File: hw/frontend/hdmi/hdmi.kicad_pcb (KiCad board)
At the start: 6 copper layers, 100 x 100 mm, 208 parts, among them J801 SAMTEC_QSH-090-D, P201 HDMI, P301 HDMI, P302 CONN_02X05, P601 CONN_02X03, P602 CONN_02X05, P801 CONN_01X02, U202 TPD12S520, U301 TPD12S521, U302 PTN3360DBS, U401 TLK3134-MULTI, U701 SI5338B, U801 ON_CAT24C256, U901 TPS54218, U902 TPS54218, U903 MIC5207-2.5YM5, U904 TPS54218, U905 FAN4860UMP

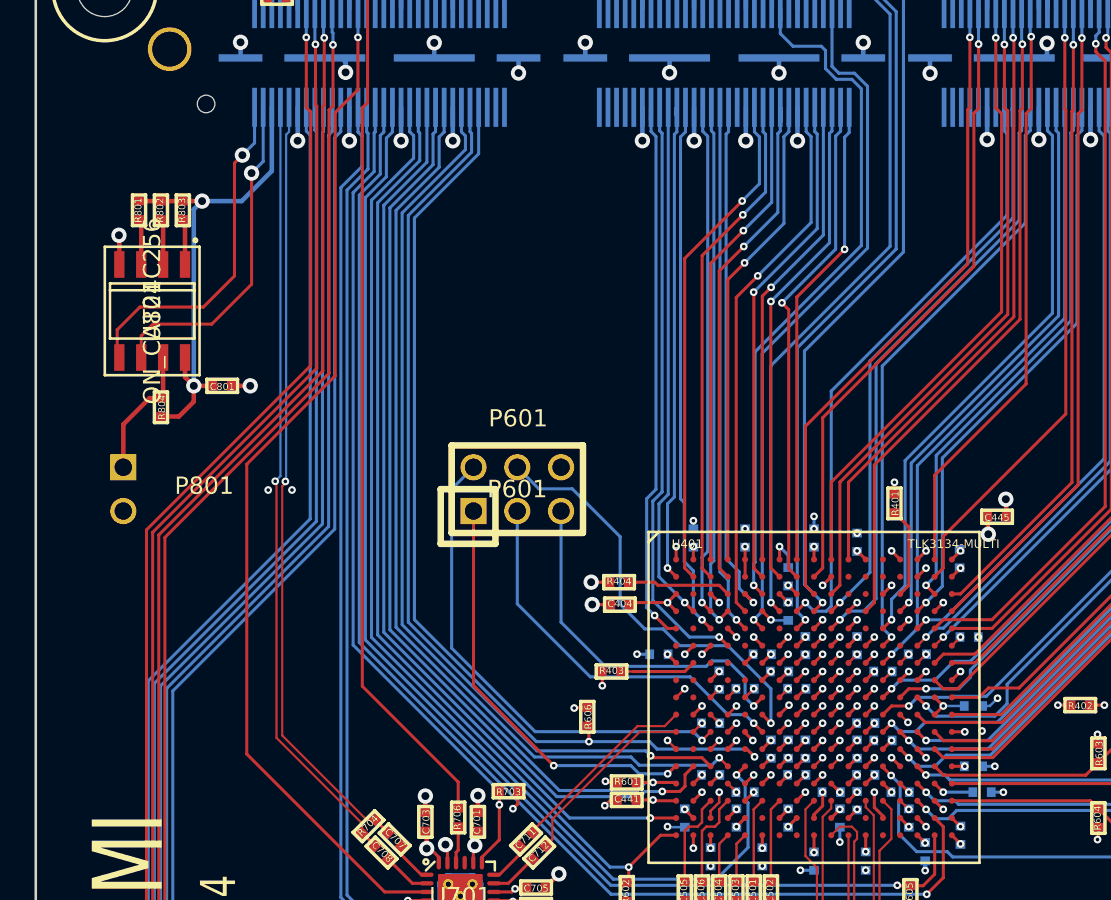
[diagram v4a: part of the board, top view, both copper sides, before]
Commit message: hdmi: improved supply zones under BGA
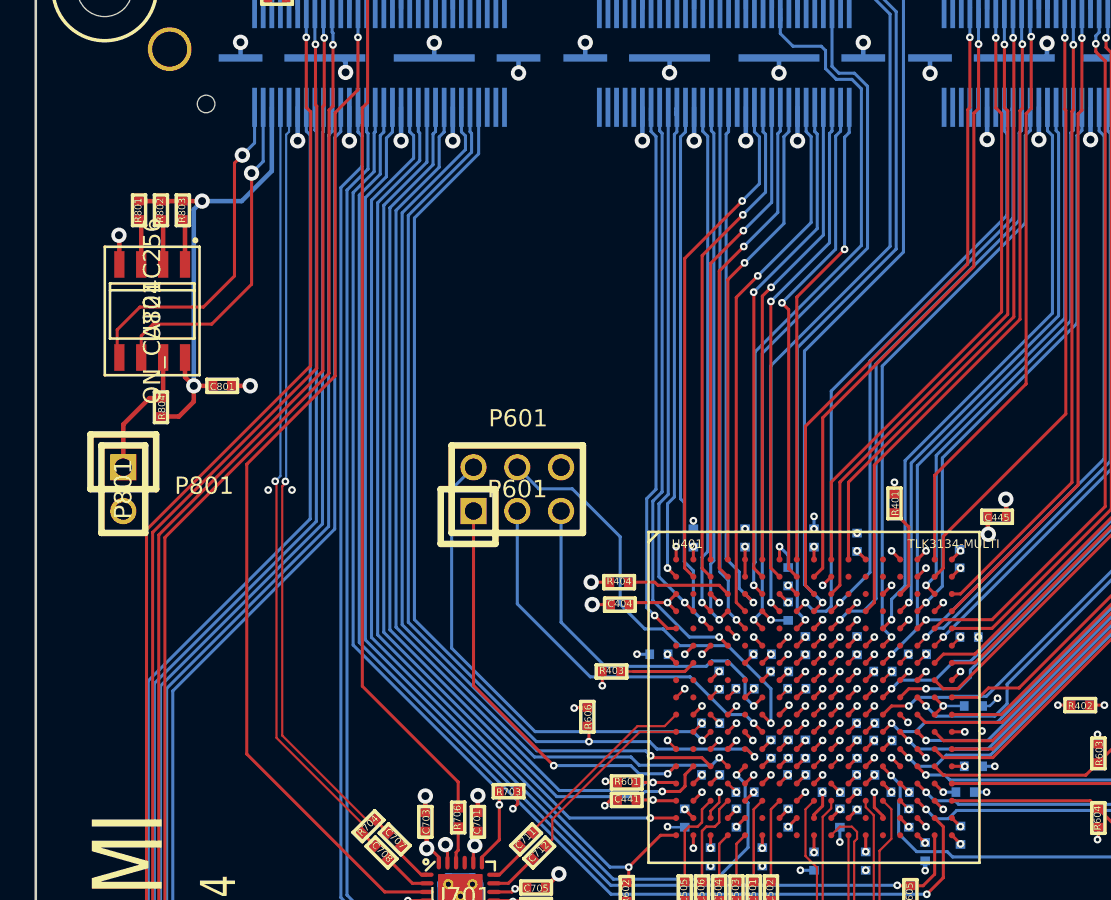
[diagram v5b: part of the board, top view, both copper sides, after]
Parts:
- P801: moved to F.Cu
- moved C437 0.98 mm to (253.9, 150.6)
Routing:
- net V2P5_REGULATED: track 64.2 -> 48.2 mm
- net V1P5_REGULATED: track 76.8 -> 71.5 mm
- net SD_CH2_RX8: track 31.8 -> 28.9 mm
- net V1P2_REGULATED: track 40.1 -> 37.3 mm
- net SD_CH1_RX3: track 29.8 -> 27.7 mm
- net SD_CH1_RX4: track 30.5 -> 28.9 mm
- net SD_CH0_RX7: track 30.6 -> 29.0 mm
- net SD_CH1_RX7: track 29.0 -> 27.7 mm

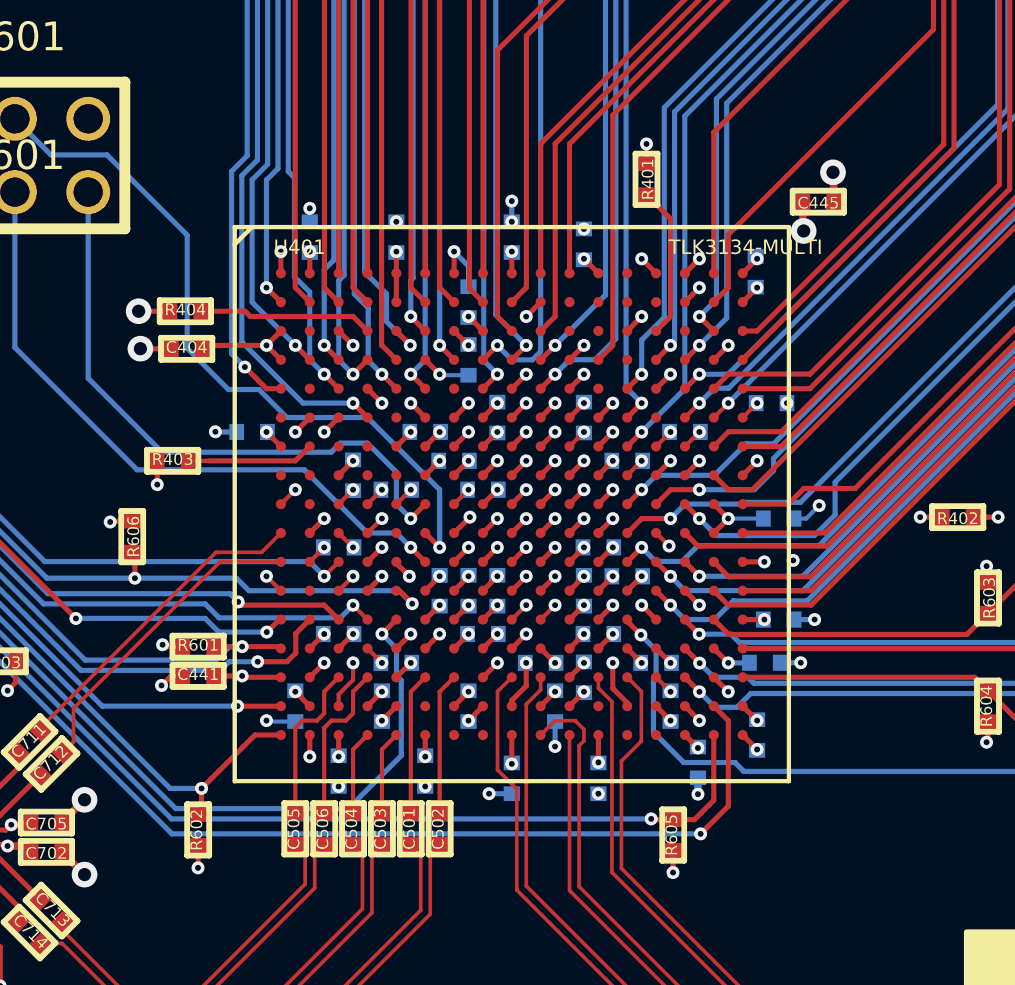
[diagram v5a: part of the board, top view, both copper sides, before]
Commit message: hdmi: eliminated via-in-pad where possible
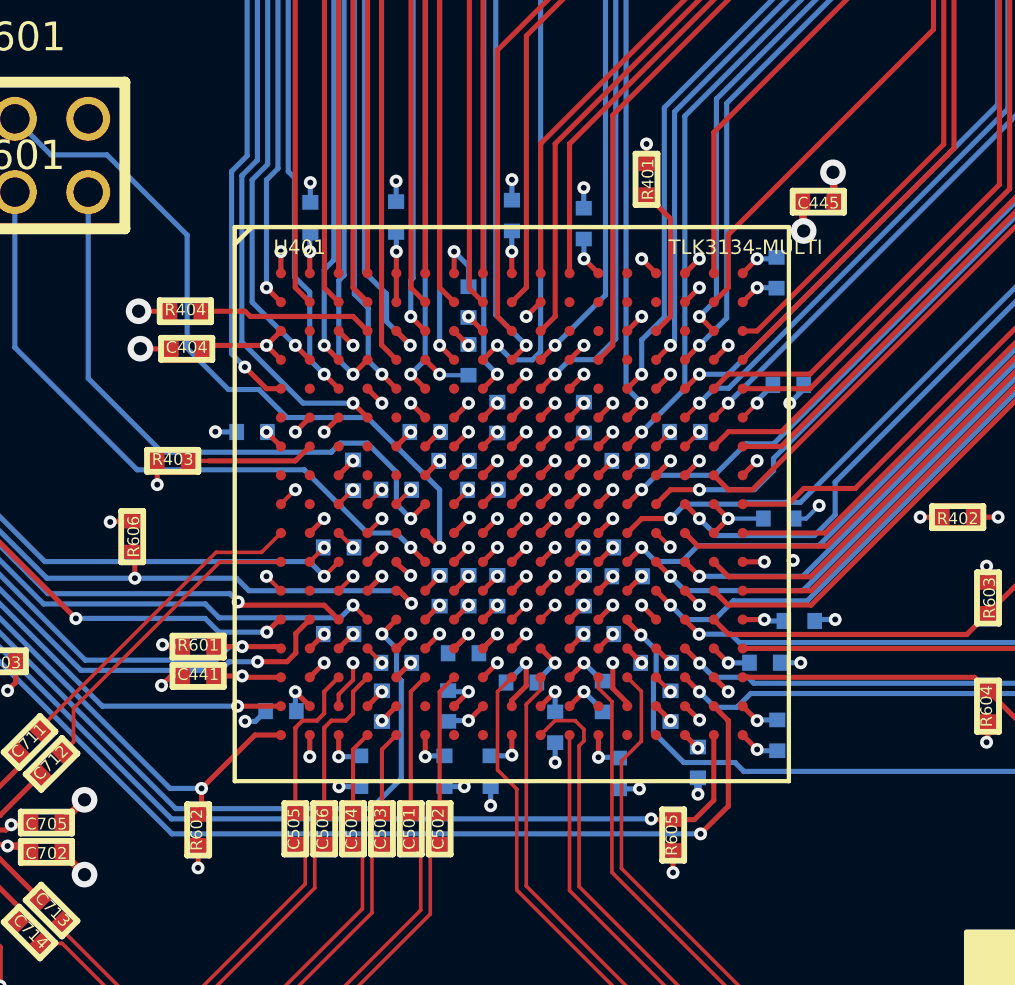
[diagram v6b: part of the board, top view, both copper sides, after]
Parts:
- moved C420 0.95 mm to (245.5, 151.3)
- moved C422 0.95 mm to (243.5, 150.3)
- moved C405 0.93 mm to (248.3, 151.8)
- moved C408 0.86 mm to (254.7, 141.0)
- moved C401 0.77 mm to (244.4, 154.4)
- moved C421 0.75 mm to (245.2, 135.1)
- moved C428 0.75 mm to (239.9, 154.4)
- moved C407 0.73 mm to (248.9, 154.4)
- moved C426 0.73 mm to (246.7, 152.8)
- moved C406 0.72 mm to (254.3, 137.1)
- moved C431 0.72 mm to (247.7, 135.4)
- moved C450 0.71 mm to (255.1, 149.1)
- moved C430 0.71 mm to (243.0, 152.1)
- moved C439 0.70 mm to (254.4, 153.1)
- moved C427 0.70 mm to (241.1, 135.2)
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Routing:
- net V1P2_REGULATED: track 37.3 -> 47.5 mm
- net GND: track 285.2 -> 295.3 mm, vias 228 -> 227
- net V1P5_REGULATED: track 71.5 -> 76.2 mm
- net V2P5_REGULATED: track 48.2 -> 48.9 mm
